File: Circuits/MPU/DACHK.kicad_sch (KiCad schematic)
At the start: 0 parts

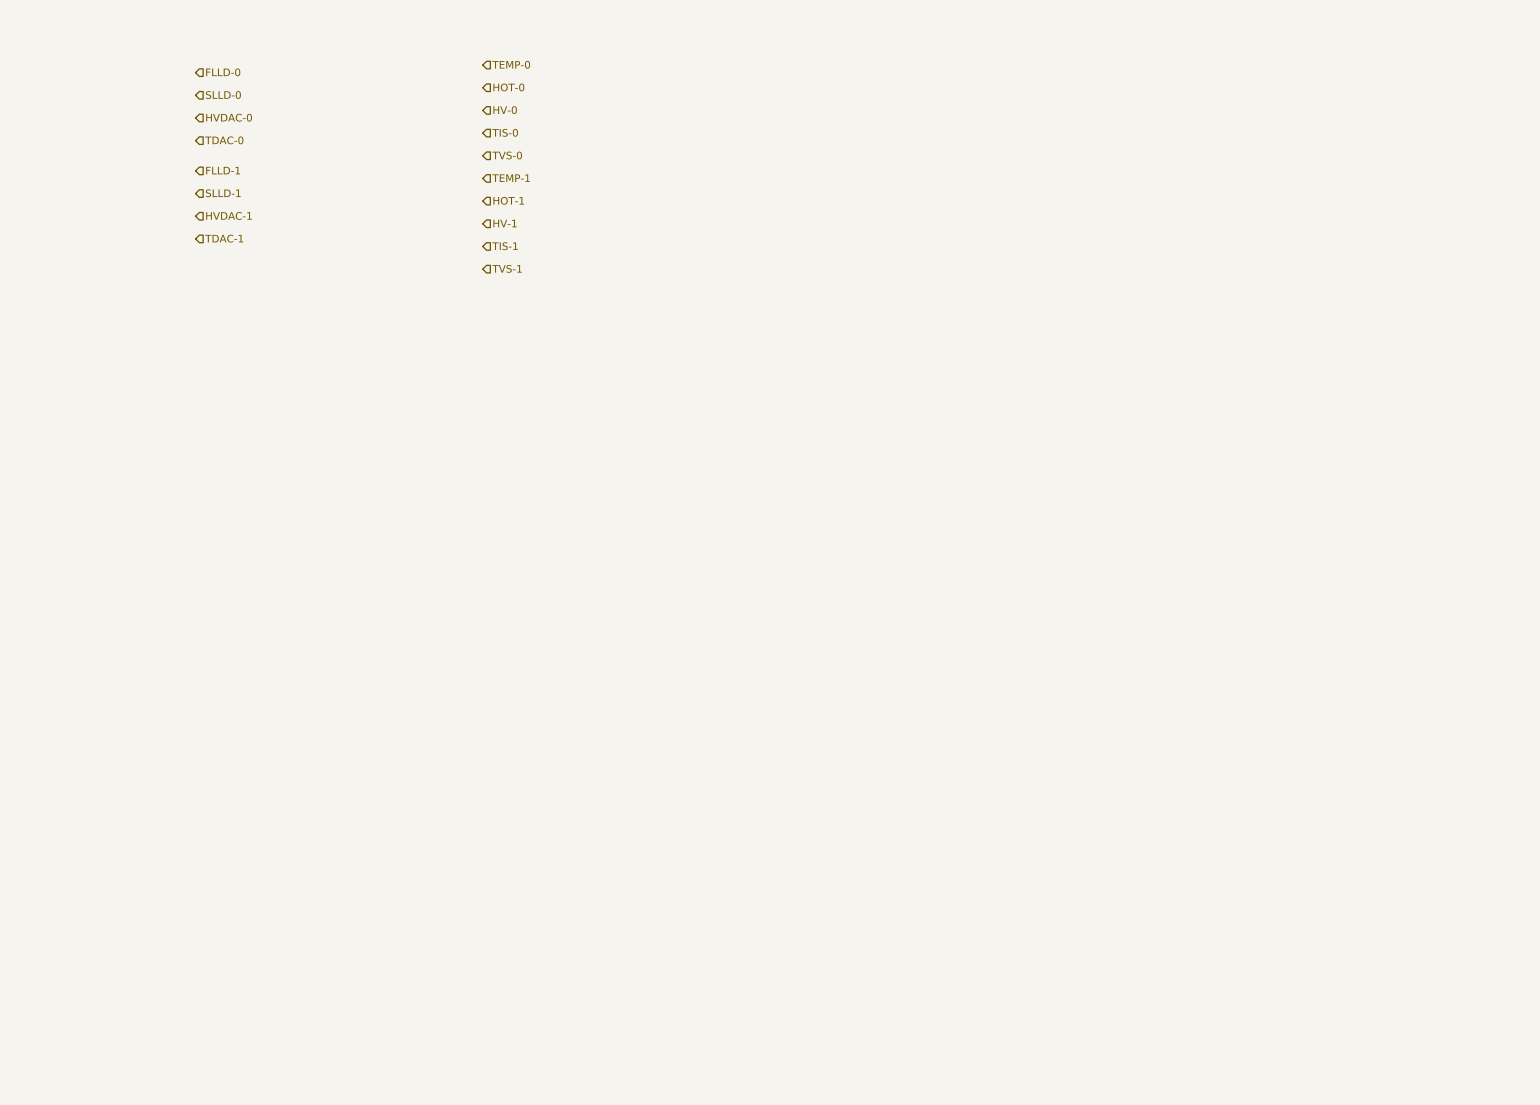
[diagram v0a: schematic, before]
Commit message: All pages populated with parts
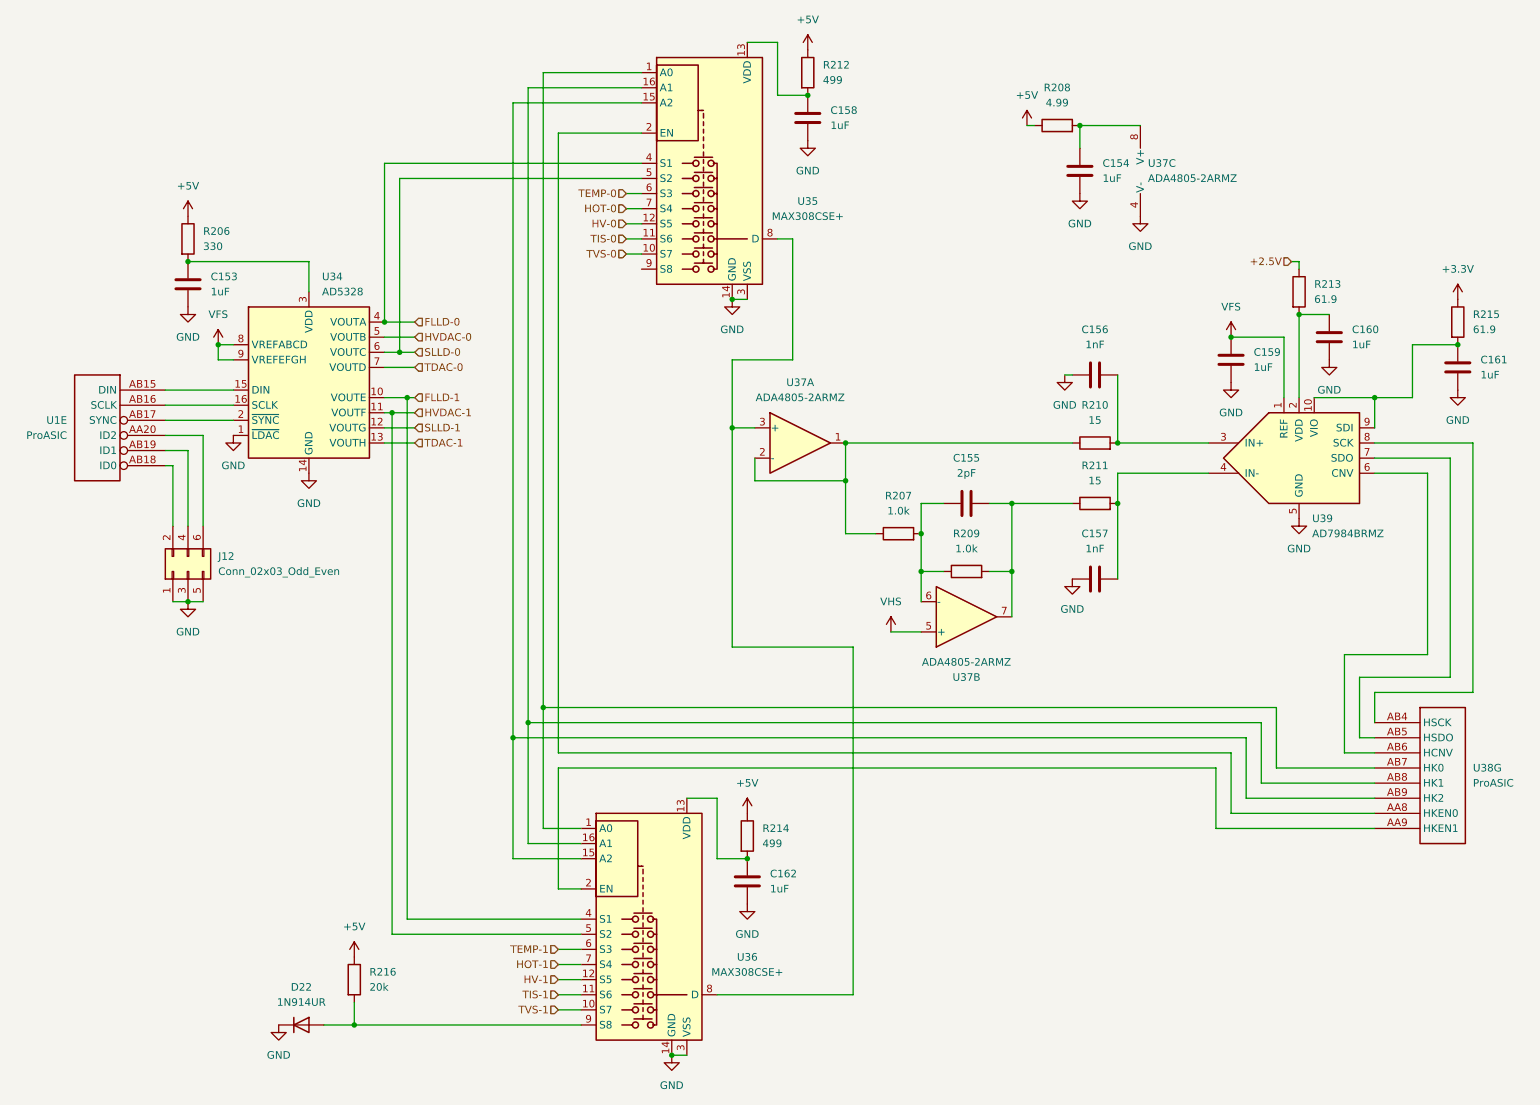
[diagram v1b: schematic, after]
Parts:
- added C153, C154, C158, C159, C160, C161, C162: 1uF, Capacitor_SMD:C_0805_2012Metric, symbol QuERI_symbols:C
- added C155: 2pF, Capacitor_SMD:C_0603_1608Metric, symbol QuERI_symbols:Csmall
- added C156, C157: 1nF, Capacitor_SMD:C_0603_1608Metric, symbol QuERI_symbols:Csmall
- added D22: 1N914UR, Diode_SMD:D_MiniMELF, symbol QuERI_symbols:1N914UR
- added J12: Conn_02x03_Odd_Even, symbol Connector_Generic:Conn_02x03_Odd_Even
- added R206: 330, Resistor_SMD:R_0603_1608Metric, symbol QuERI_symbols:Rlowp
- added R207, R209: 1.0k, Resistor_SMD:R_0603_1608Metric, symbol QuERI_symbols:Rlowp
- added R208: 4.99, Resistor_SMD:R_0603_1608Metric, symbol QuERI_symbols:Rlowp
- added R210, R211: 15, Resistor_SMD:R_0603_1608Metric, symbol QuERI_symbols:Rlowp
- added R212, R214: 499, Resistor_SMD:R_0603_1608Metric, symbol QuERI_symbols:Rlowp
- added R213, R215: 61.9, Resistor_SMD:R_0603_1608Metric, symbol QuERI_symbols:Rlowp
- added R216: 20k, Resistor_SMD:R_0603_1608Metric, symbol QuERI_symbols:Rlowp
- added U1, U38: ProASIC, Package_BGA:BGA-484_23.0x23.0mm_Layout22x22_P1.0mm, symbol QuERI_FPGA:ProASIC
- added U34: AD5328, Package_SO:TSSOP-16_4.4x5mm_P0.65mm, symbol QuERI_symbols:AD5328
- added U35, U36: MAX308CSE+, Package_SO:SO-16_3.9x9.9mm_P1.27mm, symbol QuERI_symbols:MAX308CSE+
- added U37: ADA4805-2ARMZ, Package_SO:MSOP-8_3x3mm_P0.65mm, symbol QuERI_symbols:ADA4805-2ARMZ
- added U39: AD7984BRMZ, Package_SO:MSOP-10_3x3mm_P0.5mm, symbol QuERI_symbols:AD7984BRMZ
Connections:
- net FLLD-0: now also U34.4 (VOUTA), U35.4 (S1)
- net FLLD-1: now also U34.10 (VOUTE), U36.4 (S1)
- net HOT-0: now also U35.7 (S4)
- net HOT-1: now also U36.7 (S4)
- net HV-0: now also U35.12 (S5)
- net HV-1: now also U36.12 (S5)
- net HVDAC-0: now also U34.5 (VOUTB)
- net HVDAC-1: now also U34.11 (VOUTF), U36.5 (S2)
- net SLLD-0: now also U34.6 (VOUTC), U35.5 (S2)
- net SLLD-1: now also U34.12 (VOUTG)
- net TDAC-0: now also U34.7 (VOUTD)
- net TDAC-1: now also U34.13 (VOUTH)
- net TEMP-0: now also U35.6 (S3)
- net TEMP-1: now also U36.6 (S3)
- net TIS-0: now also U35.11 (S6)
- net TIS-1: now also U36.11 (S6)
- net TVS-0: now also U35.10 (S7)
- net TVS-1: now also U36.10 (S7)
- new net: C158.1, R212.2, U35.13 (VDD)
- new net: D22.2 (A), R216.2, U36.9 (S8)
- new net: R207.1, R210.1, U37.1, U37.2 (-)
- new net: C155.1, R207.2, R209.1, U37.6 (-)
- new net: C155.2, R209.2, R211.1, U37.7
- new net: J12.6 (Pin_6), U1.AA20 (ID2)
- new net: U1.AB15 (DIN), U34.15 (DIN)
- new net: U1.AB16 (SCLK), U34.16 (SCLK)
- new net: U1.AB17 (SYNC), U34.2 (~{SYNC})
- new net: J12.2 (Pin_2), U1.AB18 (ID0)
- new net: J12.4 (Pin_4), U1.AB19 (ID1)
- new net: C153.1, R206.2, U34.3 (VDD)
- new net: C162.1, R214.2, U36.13 (VDD)
- new net: C157.2, R211.2, U39.4 (IN-)
- new net: C161.1, R215.2, U39.10 (VIO), U39.9 (SDI)
- new net: U35.8 (D), U36.8 (D), U37.3 (+)
- new net: C154.1, R208.2, U37.8 (V+)
- new net: C160.1, R213.2, U39.2 (VDD)
- new net: C156.2, R210.2, U39.3 (IN+)
- new net: U38.AB6 (HCNV), U39.6 (CNV)
- new net: U38.AB5 (HSDO), U39.7 (SDO)
- new net: U38.AB4 (HSCK), U39.8 (SCK)
- new net: U35.1 (A0), U36.1 (A0), U38.AB7 (HK0)
- new net: U35.15 (A2), U36.15 (A2), U38.AB9 (HK2)
- new net: U35.16 (A1), U36.16 (A1), U38.AB8 (HK1)
- new net: U36.2 (EN), U38.AA9 (HKEN1)
- new net: U35.2 (EN), U38.AA8 (HKEN0)
- new net +2.5V: R213.1
- new net +3.3V: R215.1
- new net +5V: R206.1, R208.1, R212.1, R214.1, R216.1
- new net GND: C153.2, C154.2, C156.1, C157.1, C158.2, C159.2, C160.2, C161.2, C162.2, D22.1 (K), J12.1 (Pin_1), J12.3 (Pin_3), J12.5 (Pin_5), U34.1 (~{LDAC}), U34.14 (GND), U35.14 (GND), U35.3 (VSS), U36.14 (GND), U36.3 (VSS), U37.4 (V-), U39.5 (GND)
- new net VFS: C159.1, U34.8 (VREFABCD), U34.9 (VREFEFGH), U39.1 (REF)
- new net VHS: U37.5 (+)

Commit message: Passes DRC
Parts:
- removed U38: ProASIC, Package_BGA:BGA-484_23.0x23.0mm_Layout22x22_P1.0mm, symbol QuERI_FPGA:ProASIC
- added unit 7 of U1
- renumbered C153 to C27, C162 to C28, C158 to C29, C155 to C30, C154 to C31, C156 to C32, C157 to C33, C159 to C34, C160 to C35, C161 to C36, D22 to D1, R206 to R63, R216 to R64, R214 to R65, R212 to R66, R207 to R67, R209 to R68, R208 to R69, R210 to R70, R211 to R71, R213 to R72, R215 to R73, U34 to U11, U36 to U12, U35 to U13, U37 to U14, U39 to U15
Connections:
- net VHS: now also U13.9 (S8)
- net ~{ID2}: now reaches J12.6 (Pin_6), U1.AA20 (ID2)
- net DIN: now reaches U1.AB15 (DIN), U11.15 (DIN)
- net SCLK: now reaches U1.AB16 (SCLK), U11.16 (SCLK)
- net ~{SYNC}: now reaches U1.AB17 (SYNC), U11.2 (~{SYNC})
- net ~{ID0}: now reaches J12.2 (Pin_2), U1.AB18 (ID0)
- net ~{ID1}: now reaches J12.4 (Pin_4), U1.AB19 (ID1)
- net HCNV: now reaches U15.6 (CNV)
- net HCNV: now also U1.AB6 (HCNV)
- net HSDO: now reaches U15.7 (SDO)
- net HSDO: now also U1.AB5 (HSDO)
- net HSCK: now reaches U15.8 (SCK)
- net HSCK: now also U1.AB4 (HSCK)
- net HK0: now reaches U12.1 (A0), U13.1 (A0)
- net HK0: now also U1.AB7 (HK0)
- net HK2: now reaches U12.15 (A2), U13.15 (A2)
- net HK2: now also U1.AB9 (HK2)
- net HK1: now reaches U12.16 (A1), U13.16 (A1)
- net HK1: now also U1.AB8 (HK1)
- net HKEN1: now reaches U12.2 (EN)
- net HKEN1: now also U1.AA9 (HKEN1)
- net HKEN0: now reaches U13.2 (EN)
- net HKEN0: now also U1.AA8 (HKEN0)
- net +2.5V renamed +2.5F
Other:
- moved on the sheet: C27, J12, R63

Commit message: bunch of little fixes
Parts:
- J12: footprint (none) -> Connector_PinHeader_2.54mm:PinHeader_2x03_P2.54mm_Vertical
- U1: footprint Package_BGA:BGA-484_23.0x23.0mm_Layout22x22_P1.0mm -> Package_BGA:BGA-484_23.0x23.0mm_Layout22x22_P1.0mm
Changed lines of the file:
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@@
 	(title_block
 		(title "QuERI MPU")
-		(date "2024-03-28")
+		(date "2024-05-26")
 		(rev "Draft")
 		(company "Noqsi Aerospace Ltd")
@@
 			)
 		)
-		(property "Footprint" "	Package_BGA:BGA-484_23.0x23.0mm_Layout22x22_P1.0mm"
+		(property "Footprint" "Package_BGA:BGA-484_23.0x23.0mm_Layout22x22_P1.0mm"
 			(at 30.48 82.55 0)
 			(effects
@@
 			)
 		)
-		(property "Footprint" "	Package_BGA:BGA-484_23.0x23.0mm_Layout22x22_P1.0mm"
+		(property "Footprint" "Package_BGA:BGA-484_23.0x23.0mm_Layout22x22_P1.0mm"
 			(at 248.92 138.43 0)
 			(effects
@@
 			)
 		)
-		(property "Footprint" ""
+		(property "Footprint" "Connector_PinHeader_2.54mm:PinHeader_2x03_P2.54mm_Vertical"
 			(at 41.91 116.84 0)
 			(effects
